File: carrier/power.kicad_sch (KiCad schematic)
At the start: 33 parts, among them U3 MP2636GR-P

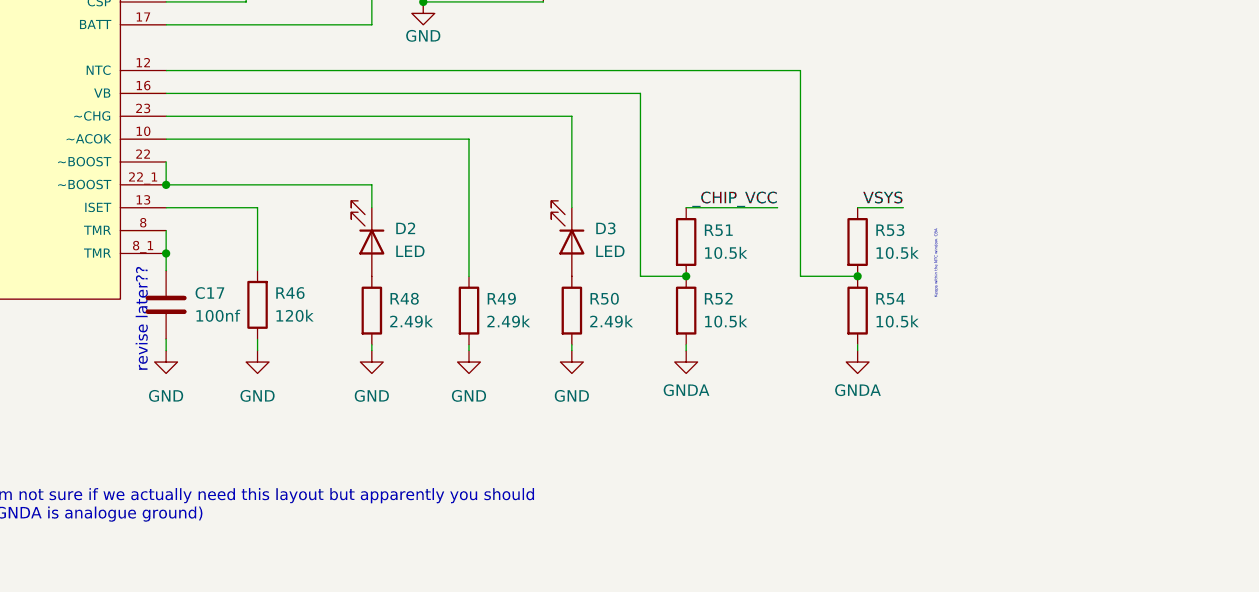
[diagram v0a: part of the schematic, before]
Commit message: getting back into the swing of this
aded some stuff for the resistors, moved some stuff about, removed the schmitt inverter (software is the solution for all our problems, forever)
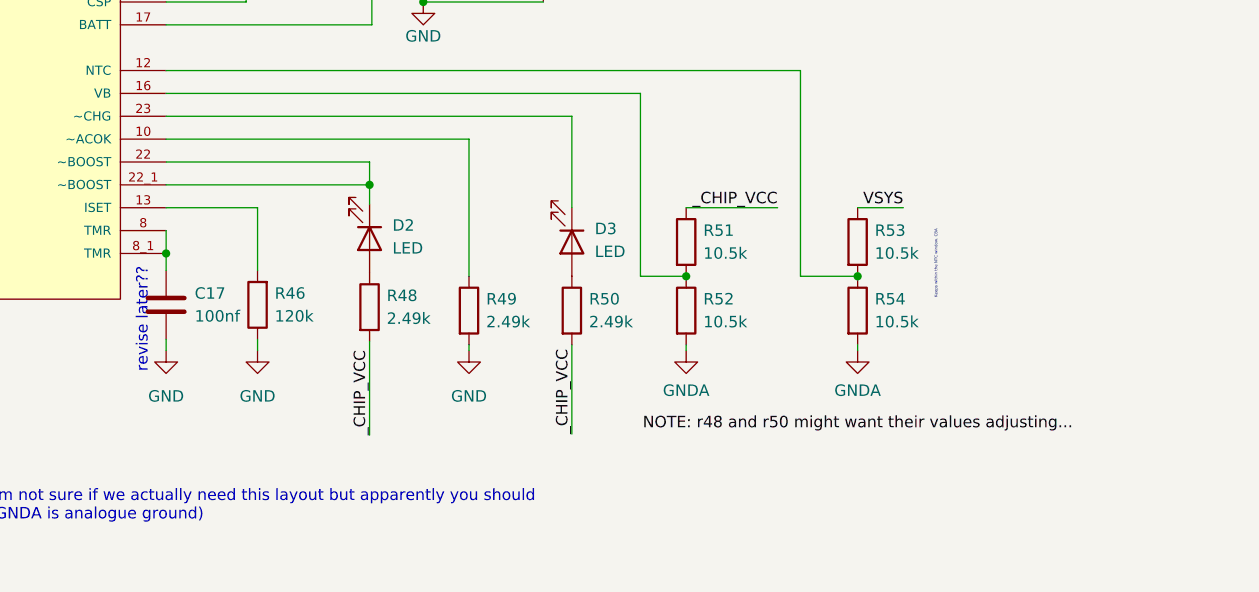
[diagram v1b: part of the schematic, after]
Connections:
- net GND: no longer R48.2, R50.2
- net _CHIP_VCC: now also R48.2, R50.2
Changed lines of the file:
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@@
   (junction (at 168.275 26.035) (diameter 0.9144) (color 0 0 0 0))
   (junction (at 175.895 55.88) (diameter 0.9144) (color 0 0 0 0))
-  (junction (at 175.895 83.82) (diameter 0.9144) (color 0 0 0 0))
   (junction (at 175.895 91.44) (diameter 0.9144) (color 0 0 0 0))
   (junction (at 179.07 26.035) (diameter 0.9144) (color 0 0 0 0))
@@
   (junction (at 184.785 55.88) (diameter 0.9144) (color 0 0 0 0))
   (junction (at 191.77 26.035) (diameter 0.9144) (color 0 0 0 0))
+  (junction (at 198.501 83.82) (diameter 0) (color 0 0 0 0))
   (junction (at 198.755 55.88) (diameter 0.9144) (color 0 0 0 0))
   (junction (at 204.47 55.88) (diameter 0.9144) (color 0 0 0 0))
@@
     (stroke (width 0) (type solid) (color 0 0 0 0))
   )
-  (wire (pts (xy 175.895 81.28) (xy 175.895 83.82))
-    (stroke (width 0) (type solid) (color 0 0 0 0))
-  )
-  (wire (pts (xy 175.895 83.82) (xy 198.755 83.82))
-    (stroke (width 0) (type solid) (color 0 0 0 0))
+  (wire (pts (xy 175.895 83.82) (xy 198.501 83.82))
+    (stroke (width 0) (type default) (color 0 0 0 0))
   )
   (wire (pts (xy 175.895 86.36) (xy 186.055 86.36))
@@
     (stroke (width 0) (type solid) (color 0 0 0 0))
   )
+  (wire (pts (xy 198.501 81.28) (xy 175.895 81.28))
+    (stroke (width 0) (type default) (color 0 0 0 0))
+  )
+  (wire (pts (xy 198.501 83.82) (xy 198.501 81.28))
+    (stroke (width 0) (type default) (color 0 0 0 0))
+  )
+  (wire (pts (xy 198.501 85.979) (xy 198.501 83.82))
+    (stroke (width 0) (type default) (color 0 0 0 0))
+  )
+  (wire (pts (xy 198.501 101.219) (xy 198.501 111.633))
+    (stroke (width 0) (type default) (color 0 0 0 0))
+  )
   (wire (pts (xy 198.755 55.88) (xy 204.47 55.88))
     (stroke (width 0) (type solid) (color 0 0 0 0))
@@
     (stroke (width 0) (type solid) (color 0 0 0 0))
   )
-  (wire (pts (xy 198.755 83.82) (xy 198.755 86.36))
-    (stroke (width 0) (type solid) (color 0 0 0 0))
-  )
-  (wire (pts (xy 198.755 101.6) (xy 198.755 102.235))
-    (stroke (width 0) (type solid) (color 0 0 0 0))
-  )
   (wire (pts (xy 204.47 55.88) (xy 217.805 55.88))
     (stroke (width 0) (type solid) (color 0 0 0 0))
@@
     (stroke (width 0) (type solid) (color 0 0 0 0))
   )
-  (wire (pts (xy 220.98 101.6) (xy 220.98 102.235))
+  (wire (pts (xy 220.98 101.6) (xy 220.98 111.506))
     (stroke (width 0) (type solid) (color 0 0 0 0))
   )
@@
     (effects (font (size 1.27 1.27)) (justify left bottom))
   )
+  (label "_CHIP_VCC" (at 198.501 111.633 90)
+    (effects (font (size 1.27 1.27)) (justify left bottom))
+  )
   (label "VSYS" (at 201.93 26.035 180)
     (effects (font (size 1.27 1.27)) (justify right bottom))
   )
+  (label "_CHIP_VCC" (at 220.98 111.506 90)
+    (effects (font (size 1.27 1.27)) (justify left bottom))
+  )
+  (label "NOTE: r48 and r50 might want their values adjusting..."
+    (at 228.854 111.252 0)
+    (effects (font (size 1.27 1.27)) (justify left bottom))
+  )
   (label "_CHIP_VCC" (at 243.84 86.36 180)
     (effects (font (size 1.27 1.27)) (justify right bottom))
@@
     (pin "1")
   )
-  (symbol (lib_id "power:GND") (at 198.755 102.235 0) (unit 1)
-    (in_bom yes) (on_board yes) (fields_autoplaced)
-    (property "Reference" "#PWR037" (id 0) (at 198.755 108.585 0)
-      (effects (font (size 1.27 1.27)) hide)
-    )
-    (property "Value" "GND" (id 1) (at 198.755 107.315 0))
-    (property "Footprint" "" (id 2) (at 198.755 102.235 0)
-      (effects (font (size 1.27 1.27)) hide)
-    )
-    (property "Datasheet" "" (id 3) (at 198.755 102.235 0)
-      (effects (font (size 1.27 1.27)) hide)
-    )
-    (pin "1")
-  )
   (symbol (lib_id "power:GND") (at 204.47 63.5 0) (unit 1)
     (in_bom yes) (on_board yes)
@@
     )
     (property "Datasheet" "" (id 3) (at 209.55 102.235 0)
-      (effects (font (size 1.27 1.27)) hide)
-    )
-    (pin "1")
-  )
-  (symbol (lib_id "power:GND") (at 220.98 102.235 0) (unit 1)
-    (in_bom yes) (on_board yes) (fields_autoplaced)
-    (property "Reference" "#PWR040" (id 0) (at 220.98 108.585 0)
-      (effects (font (size 1.27 1.27)) hide)
-    )
-    (property "Value" "GND" (id 1) (at 220.98 107.315 0))
-    (property "Footprint" "" (id 2) (at 220.98 102.235 0)
-      (effects (font (size 1.27 1.27)) hide)
-    )
-    (property "Datasheet" "" (id 3) (at 220.98 102.235 0)
       (effects (font (size 1.27 1.27)) hide)
     )
@@
     (pin "2")
   )
-  (symbol (lib_id "Device:R") (at 198.755 97.79 0) (unit 1)
-    (in_bom yes) (on_board yes) (fields_autoplaced)
-    (property "Reference" "R48" (id 0) (at 200.66 96.5199 0)
-      (effects (font (size 1.27 1.27)) (justify left))
-    )
-    (property "Value" "2.49k" (id 1) (at 200.66 99.0599 0)
-      (effects (font (size 1.27 1.27)) (justify left))
-    )
-    (property "Footprint" "Resistor_SMD:R_0402_1005Metric_Pad0.72x0.64mm_HandSolder" (id 2) (at 196.977 97.79 90)
-      (effects (font (size 1.27 1.27)) hide)
-    )
-    (property "Datasheet" "~" (id 3) (at 198.755 97.79 0)
+  (symbol (lib_id "Device:R") (at 198.501 97.409 0) (unit 1)
+    (in_bom yes) (on_board yes) (fields_autoplaced)
+    (property "Reference" "R48" (id 0) (at 200.406 96.1389 0)
+      (effects (font (size 1.27 1.27)) (justify left))
+    )
+    (property "Value" "2.49k" (id 1) (at 200.406 98.6789 0)
+      (effects (font (size 1.27 1.27)) (justify left))
+    )
+    (property "Footprint" "Resistor_SMD:R_0402_1005Metric_Pad0.72x0.64mm_HandSolder" (id 2) (at 196.723 97.409 90)
+      (effects (font (size 1.27 1.27)) hide)
+    )
+    (property "Datasheet" "~" (id 3) (at 198.501 97.409 0)
       (effects (font (size 1.27 1.27)) hide)
     )
@@
     (pin "2")
   )
-  (symbol (lib_id "Device:LED") (at 198.755 90.17 270) (unit 1)
-    (in_bom yes) (on_board yes) (fields_autoplaced)
-    (property "Reference" "D2" (id 0) (at 201.295 88.7094 90)
-      (effects (font (size 1.27 1.27)) (justify left))
-    )
-    (property "Value" "LED" (id 1) (at 201.295 91.2494 90)
-      (effects (font (size 1.27 1.27)) (justify left))
-    )
-    (property "Footprint" "LED_SMD:LED_0805_2012Metric_Pad1.15x1.40mm_HandSolder" (id 2) (at 198.755 90.17 0)
-      (effects (font (size 1.27 1.27)) hide)
-    )
-    (property "Datasheet" "~" (id 3) (at 198.755 90.17 0)
-      (effects (font (size 1.27 1.27)) hide)
-    )
+  (symbol (lib_id "Device:LED") (at 198.501 89.789 270) (unit 1)
+    (in_bom yes) (on_board yes) (fields_autoplaced)
+    (property "Reference" "D2" (id 0) (at 201.041 88.3284 90)
+      (effects (font (size 1.27 1.27)) (justify left))
+    )
+    (property "Value" "LED" (id 1) (at 201.041 90.8684 90)
+      (effects (font (size 1.27 1.27)) (justify left))
+    )
+    (property "Footprint" "LED_SMD:LED_0805_2012Metric_Pad1.15x1.40mm_HandSolder" (id 2) (at 198.501 89.789 0)
+      (effects (font (size 1.27 1.27)) hide)
+    )
+    (property "Datasheet" "~" (id 3) (at 198.501 89.789 0)
+      (effects (font (size 1.27 1.27)) hide)
+    )

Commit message: we are nearing completion for this version
maybe one day we will make a second version
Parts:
- R40, R41, R43, R44, R45: footprint Resistor_SMD:R_0603_1608Metric_Pad0.98x0.95mm_HandSolder -> Resistor_SMD:R_0402_1005Metric_Pad0.72x0.64mm_HandSolder
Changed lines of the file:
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@@
     (property "Reference" "R40" (id 0) (at 93.98 78.105 90))
     (property "Value" "10.5k" (id 1) (at 93.98 80.01 90))
-    (property "Footprint" "Resistor_SMD:R_0603_1608Metric_Pad0.98x0.95mm_HandSolder" (id 2) (at 93.98 81.788 90)
+    (property "Footprint" "Resistor_SMD:R_0402_1005Metric_Pad0.72x0.64mm_HandSolder" (id 2) (at 93.98 81.788 90)
       (effects (font (size 1.27 1.27)) hide)
     )
@@
     (property "Reference" "R41" (id 0) (at 93.98 83.82 90))
     (property "Value" "10.5k" (id 1) (at 93.98 85.725 90))
-    (property "Footprint" "Resistor_SMD:R_0603_1608Metric_Pad0.98x0.95mm_HandSolder" (id 2) (at 93.98 87.503 90)
+    (property "Footprint" "Resistor_SMD:R_0402_1005Metric_Pad0.72x0.64mm_HandSolder" (id 2) (at 93.98 87.503 90)
       (effects (font (size 1.27 1.27)) hide)
     )
@@
     (property "Reference" "R43" (id 0) (at 143.51 34.29 90))
     (property "Value" "10k" (id 1) (at 143.51 36.83 90))
-    (property "Footprint" "Resistor_SMD:R_0603_1608Metric_Pad0.98x0.95mm_HandSolder" (id 2) (at 143.51 35.052 90)
+    (property "Footprint" "Resistor_SMD:R_0402_1005Metric_Pad0.72x0.64mm_HandSolder" (id 2) (at 143.51 35.052 90)
       (effects (font (size 1.27 1.27)) hide)
     )
@@
     (property "Reference" "R44" (id 0) (at 152.4 34.29 90))
     (property "Value" "3k" (id 1) (at 152.4 36.83 90))
-    (property "Footprint" "Resistor_SMD:R_0603_1608Metric_Pad0.98x0.95mm_HandSolder" (id 2) (at 152.4 38.608 90)
+    (property "Footprint" "Resistor_SMD:R_0402_1005Metric_Pad0.72x0.64mm_HandSolder" (id 2) (at 152.4 38.608 90)
       (effects (font (size 1.27 1.27)) hide)
     )
@@
       (effects (font (size 1.27 1.27)) (justify right))
     )
-    (property "Footprint" "Resistor_SMD:R_0603_1608Metric_Pad0.98x0.95mm_HandSolder" (id 2) (at 166.243 41.91 90)
+    (property "Footprint" "Resistor_SMD:R_0402_1005Metric_Pad0.72x0.64mm_HandSolder" (id 2) (at 166.243 41.91 90)
       (effects (font (size 1.27 1.27)) hide)
     )

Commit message: getting there!!
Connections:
- net GND: no longer R44.2, R45.2
- net __CSP: now reaches L1.2, R47.1, U3.18 (CSP)
- net __SW: now reaches L1.1, U3.2 (SW), U3.21 (SW)
- new net: R44.2, R45.2
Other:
- note added: "Keeps within the NTC window. CBA (For future reference, this is for temperature. You can use a thermistor and chip turn off too hot"
- note removed: "Keeps within the NTC window. CBA"
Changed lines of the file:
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@@
     (effects (font (size 1.27 1.27)) (justify left bottom))
   )
-  (text "Keeps within the NTC window. CBA" (at 261.62 88.9 270)
+  (text "Keeps within the NTC window. CBA\n(For future reference, this is for temperature. You can use a thermistor and chip turn off too hot"
+    (at 261.62 88.9 90)
     (effects (font (size 0.3175 0.3175)) (justify right bottom))
   )
   (label "_CHIP_VCC" (at 66.04 74.93 0)
+    (effects (font (size 1.27 1.27)) (justify left bottom))
+  )
+  (label "__SW" (at 176.657 55.88 0)
+    (effects (font (size 1.27 1.27)) (justify left bottom))
+  )
+  (label "__CSP" (at 185.42 55.88 0)
     (effects (font (size 1.27 1.27)) (justify left bottom))
   )
@@
     (pin "1")
   )
-  (symbol (lib_id "power:GND") (at 156.845 38.735 0) (unit 1)
-    (in_bom yes) (on_board yes) (fields_autoplaced)
-    (property "Reference" "#PWR033" (id 0) (at 156.845 45.085 0)
-      (effects (font (size 1.27 1.27)) hide)
-    )
-    (property "Value" "GND" (id 1) (at 156.845 43.18 0))
-    (property "Footprint" "" (id 2) (at 156.845 38.735 0)
-      (effects (font (size 1.27 1.27)) hide)
-    )
-    (property "Datasheet" "" (id 3) (at 156.845 38.735 0)
-      (effects (font (size 1.27 1.27)) hide)
-    )
+  (symbol (lib_id "power:GNDA") (at 156.718 38.735 0) (unit 1)
+    (in_bom yes) (on_board yes) (fields_autoplaced)
+    (property "Reference" "#PWR0109" (id 0) (at 156.718 45.085 0)
+      (effects (font (size 1.27 1.27)) hide)
+    )
+    (property "Value" "GNDA" (id 1) (at 156.718 43.18 0))
+    (property "Footprint" "" (id 2) (at 156.718 38.735 0)
+      (effects (font (size 1.27 1.27)) hide)
+    )
+    (property "Datasheet" "" (id 3) (at 156.718 38.735 0)
+      (effects (font (size 1.27 1.27)) hide)
+    )

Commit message: Auto stash before merge of "master" and "origin/master"
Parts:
- removed C15: 10uF, Capacitor_SMD:C_1206_3216Metric_Pad1.33x1.80mm_HandSolder, symbol Device:C
- removed C16: 100nF, Capacitor_SMD:C_0603_1608Metric_Pad1.08x0.95mm_HandSolder, symbol Device:C
- removed C17: 100nf, Capacitor_SMD:C_0402_1005Metric_Pad0.74x0.62mm_HandSolder, symbol Device:C
- removed C18: 22u, Capacitor_SMD:C_1206_3216Metric_Pad1.33x1.80mm_HandSolder, symbol Device:C
- removed C19, C20, C25, C26: 10u, Capacitor_SMD:C_1206_3216Metric_Pad1.33x1.80mm_HandSolder, symbol Device:C
- removed D2, D3: LED, LED_SMD:LED_0805_2012Metric_Pad1.15x1.40mm_HandSolder, symbol Device:LED
- removed L1: 6.8uH, Inductor_SMD:L_Wuerth_WE-PD-Typ-M-Typ-S_Handsoldering, symbol Device:L
- removed NT1: NetTie, NetTie:NetTie-2_SMD_Pad0.5mm, symbol Device:NetTie_2
- removed R36, R39: 1k, Resistor_SMD:R_0402_1005Metric_Pad0.72x0.64mm_HandSolder, symbol Device:R
- removed R37: 9k, Resistor_SMD:R_0402_1005Metric_Pad0.72x0.64mm_HandSolder, symbol Device:R
- removed R38: 1.3k, Resistor_SMD:R_0402_1005Metric_Pad0.72x0.64mm_HandSolder, symbol Device:R
- removed R40, R41, R51, R52, R53, R54: 10.5k, Resistor_SMD:R_0402_1005Metric_Pad0.72x0.64mm_HandSolder, symbol Device:R
- removed R42: 16k, Resistor_SMD:R_0402_1005Metric_Pad0.72x0.64mm_HandSolder, symbol Device:R
- removed R43: 10k, Resistor_SMD:R_0402_1005Metric_Pad0.72x0.64mm_HandSolder, symbol Device:R
- removed R44: 3k, Resistor_SMD:R_0402_1005Metric_Pad0.72x0.64mm_HandSolder, symbol Device:R
- removed R45: 55.2k, Resistor_SMD:R_0402_1005Metric_Pad0.72x0.64mm_HandSolder, symbol Device:R
- removed R46: 120k, Resistor_SMD:R_0402_1005Metric_Pad0.72x0.64mm_HandSolder, symbol Device:R
- removed R47: 20m, Resistor_SMD:R_2816_7142Metric_Pad3.20x4.45mm_HandSolder, symbol Device:R
- removed R48, R49, R50: 2.49k, Resistor_SMD:R_0402_1005Metric_Pad0.72x0.64mm_HandSolder, symbol Device:R
- removed TP19: +5v Output, TestPoint:TestPoint_Pad_1.0x1.0mm, symbol Connector:TestPoint
- removed U3: MP2636GR-P, mp2636:IC_MP2636GR-P, symbol mp2636:MP2636GR-P
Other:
- note removed: "BATT will be a 3000mAh 3.7v nomimal LiPo battery (if we can get larger will do) (reckon we can squeeze a 4200mAh in with some modifications (gut out the battery cage, min)"
- note removed: "Based of the MP2636 datasheet."
- note removed: "I'm not sure if we actually need this layout but apparently you should (GNDA is analogue ground)"
- note removed: "Keeps within the NTC window. CBA (For future reference, this is for temperature. You can use a thermistor and chip turn off too hot"
- note removed: "chip VCC is the INTERNAL supply!"
- note removed: "revise later??"
- note removed: "selected for worst case"
- note removed: "some figures so dont need to keep hunting for f(sw)=600khz"
- note removed: "voltage divider for set undervoltage"

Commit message: a
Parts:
- added C? (x6): C, symbol Device:C
- added L? (x2): L, symbol Device:L
- added U? (x2): TPS61253A, symbol CM4IO:TPS61253A
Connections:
- new net: C?.1, C?.1, L?.1, U?. (VOUT) (x2)
- new net: L?.2, U?. (VOUT) (x2)
- new net 3v3: C?.1, U?. (VOUT)
- new net 5v0: C?.1, U?. (VOUT)
- new net GND: C?.2, C?.2, C?.2, C?.2, C?.2, C?.2, U?. (VOUT), U?. (VOUT)
- new net PWR: U?. (VOUT), U?. (VOUT)
